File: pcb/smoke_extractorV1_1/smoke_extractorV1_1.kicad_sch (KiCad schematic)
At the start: 25 parts

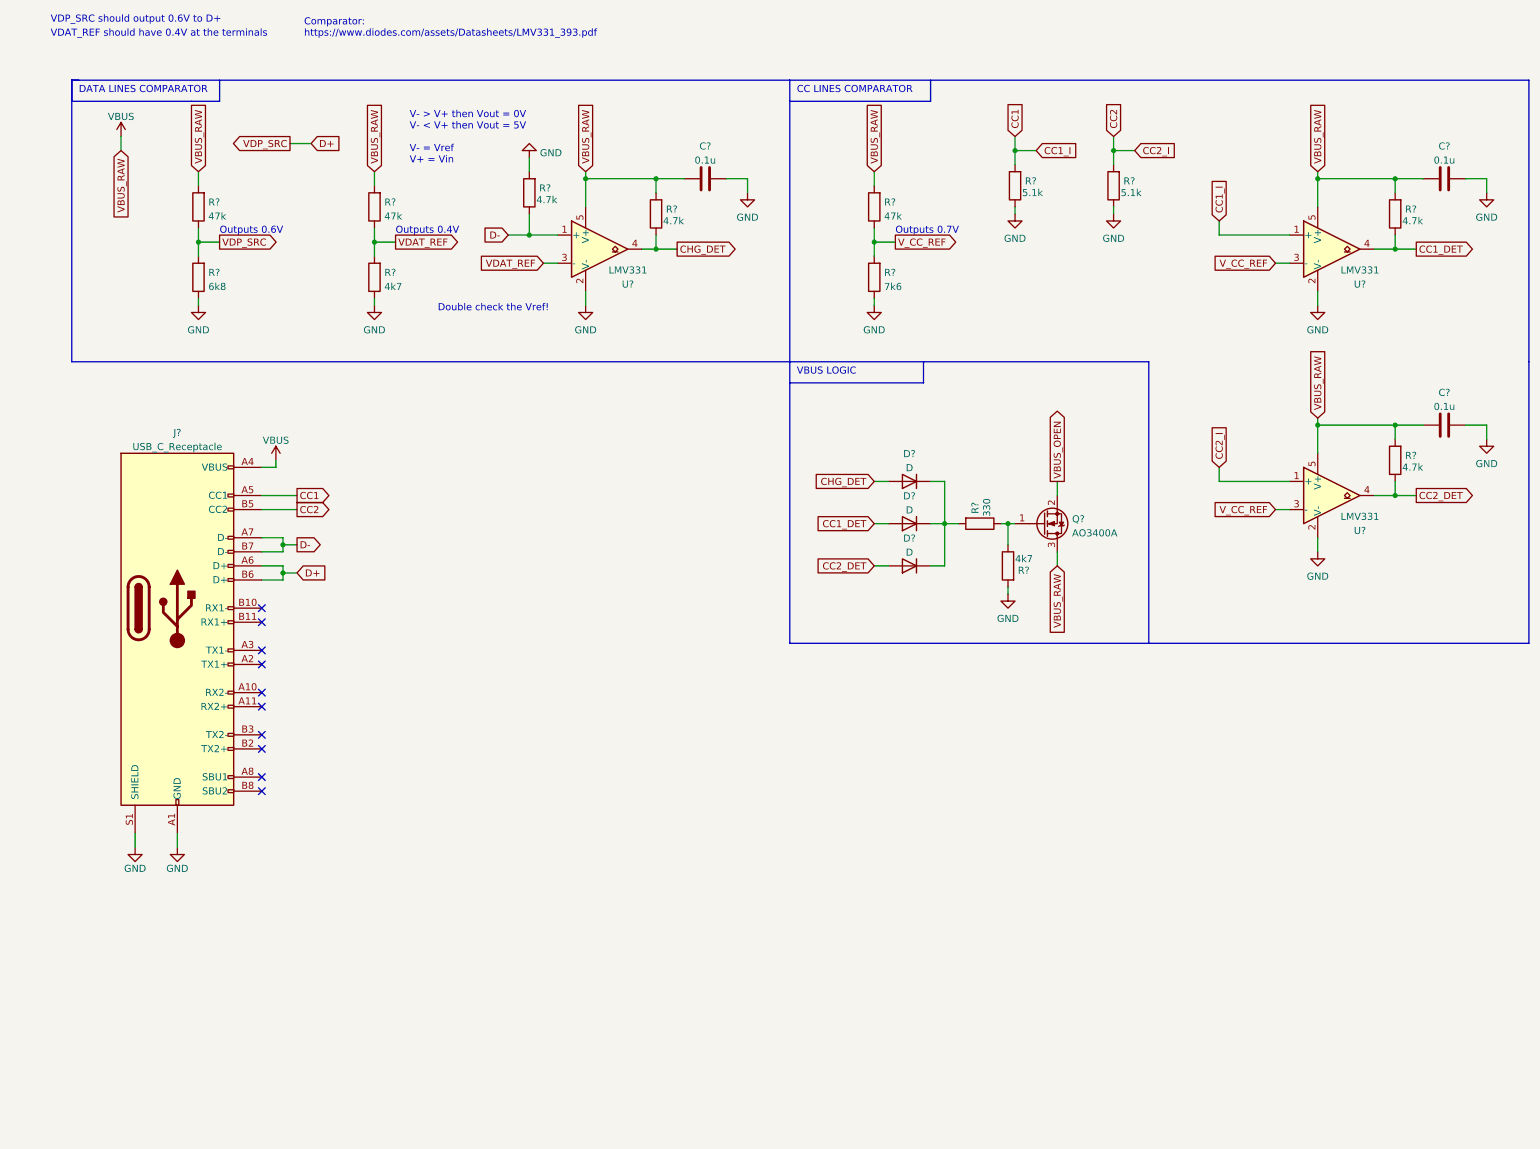
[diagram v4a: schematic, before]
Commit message: Added boost symbol + circuit
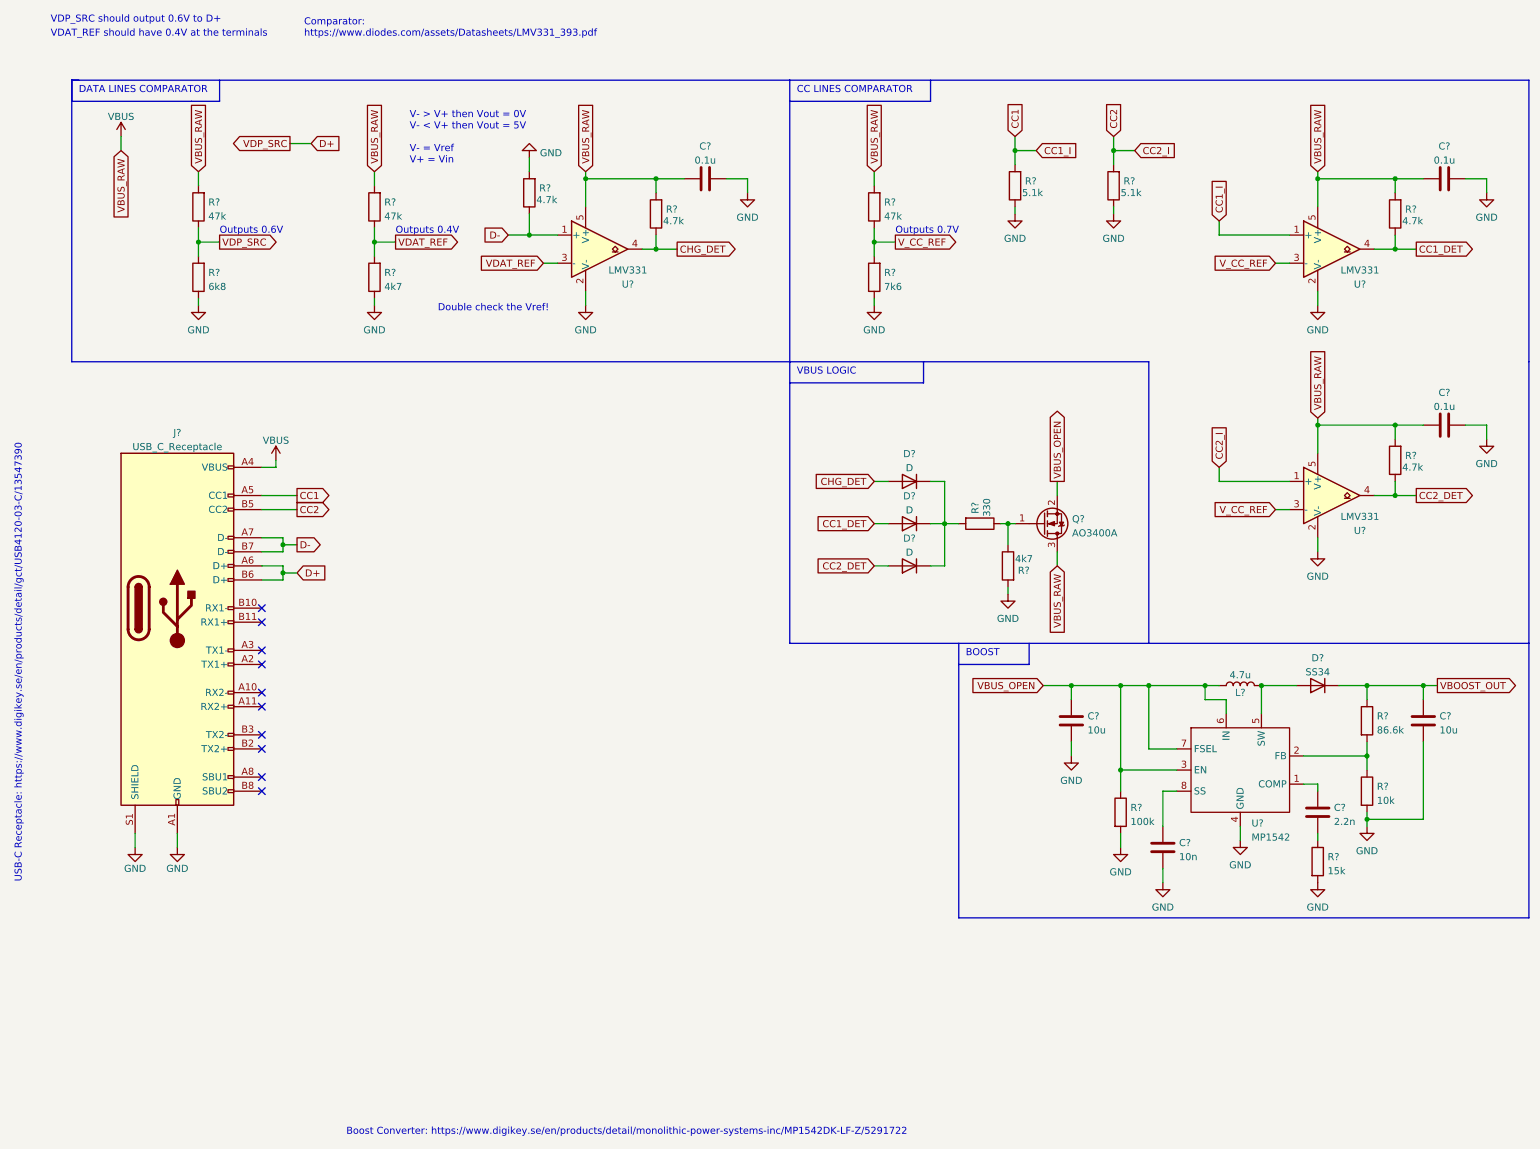
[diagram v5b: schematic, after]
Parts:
- added C?: 2.2n, symbol Device:C
- added C? (x2): 10u, symbol Device:C
- added C?: 10n, symbol Device:C
- added D?: SS34, symbol Device:D
- added L?: 4.7u, symbol Device:L
- added R?: 86.6k, symbol Device:R
- added R?: 15k, symbol Device:R
- added R?: 100k, symbol Device:R
- added R?: 10k, symbol Device:R
- added U?: MP1542, symbol CustomSymbols:MP1542
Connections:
- net GND: now also C?.2, C?.2, C?.2, R?.2, R?.2, R?.2, U?.4 (GND)
- net VBUS_OPEN: now also C?.1, L?.1, R?.1, U?.3 (EN), U?.6 (IN), U?.7 (FSEL)
- new net: C?.1, U?.1 (COMP)
- new net: R?.1, R?.2, U?.2 (FB)
- new net: D?.2 (A), L?.2, U?.5 (SW)
- new net: C?.1, U?.8 (SS)
- new net: C?.2, R?.1
- new net VBOOST_OUT: C?.1, D?.1 (K), R?.1
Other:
- note added: "BOOST"
- note added: "Boost Converter: https://www.digikey.se/en/products/detail/monolithic-power-systems-inc/MP1542DK-LF-Z/5291722"
- note added: "USB-C Receptacle: https://www.digikey.se/en/products/detail/gct/USB4120-03-C/13547390"

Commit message: Final schematics tweaks and BOM
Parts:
- added D?: LED, symbol Device:LED
- added H? (x4): MountingHole_Pad, symbol Mechanical:MountingHole_Pad
- added J?: Screw_Terminal_01x02, symbol Connector:Screw_Terminal_01x02
- added R?: 86.6k, symbol Device:R
- added U?: RA11131100, symbol CustomSymbols:RA11131100
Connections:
- net GND: now also D?.1 (K), H?.1, H?.1, H?.1, H?.1, J?.2 (Pin_2)
- net VBOOST_OUT: now also J?.1 (Pin_1)
- net VBUS_OPEN: now also U?.1 (IN); no longer C?.1, L?.1, R?.1, U?.3 (EN), U?.6 (IN), U?.7 (FSEL)
- new net: D?.2 (A), R?.2
- new net VBUS_SWITCH: C?.1, L?.1, R?.1, R?.1, U?.2 (OUT), U?.3 (EN), U?.6 (IN), U?.7 (FSEL)
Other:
- note added: "MOUNTING HOLES"
- note added: "OUTPUT"
- note added: "SWITCH"
- moved on the sheet: C?

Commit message: Ready to start designing!
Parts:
- C1, C3, C4, C6, C7: renamed from C?; footprint (none) -> Capacitor_SMD:C_0603_1608Metric_Pad1.08x0.95mm_HandSolder
- C2, C5: renamed from C?; footprint (none) -> Capacitor_SMD:C_0805_2012Metric_Pad1.18x1.45mm_HandSolder
- D1, D2, D3: renamed from D?; footprint (none) -> Diode_SMD:D_SOD-523
- D4: renamed from D?; footprint (none) -> LED_SMD:LED_0201_0603Metric_Pad0.64x0.40mm_HandSolder
- D5: renamed from D?; footprint (none) -> Diode_SMD:Nexperia_CFP3_SOD-123W
- H1, H2, H3, H4: renamed from H?; footprint (none) -> MountingHole:MountingHole_3.2mm_M3_ISO7380_Pad
- J1: renamed from J?; footprint (none) -> CustomFootprints:USB4120-03-C
- J2: renamed from J?; footprint (none) -> TerminalBlock:TerminalBlock_bornier-2_P5.08mm
- L1: renamed from L?; footprint (none) -> Inductor_SMD:L_1008_2520Metric_Pad1.43x2.20mm_HandSolder
- R1, R10, R11, R12, R13, R14, R15, R16, R17, R18, R19, R2, R3, R4, R5, R6, R7, R8, R9: renamed from R?; footprint (none) -> Resistor_SMD:R_0603_1608Metric_Pad0.98x0.95mm_HandSolder
- U1, U4, U5: renamed from U?; footprint (none) -> Package_TO_SOT_SMD:SOT-353_SC-70-5_Handsoldering
- U2: renamed from U?; footprint (none) -> CustomFootprints:RA11131100
- U3: renamed from U?; footprint (none) -> Package_SO:MSOP-8_3x3mm_P0.65mm
- gave numbers to parts that had none: 1

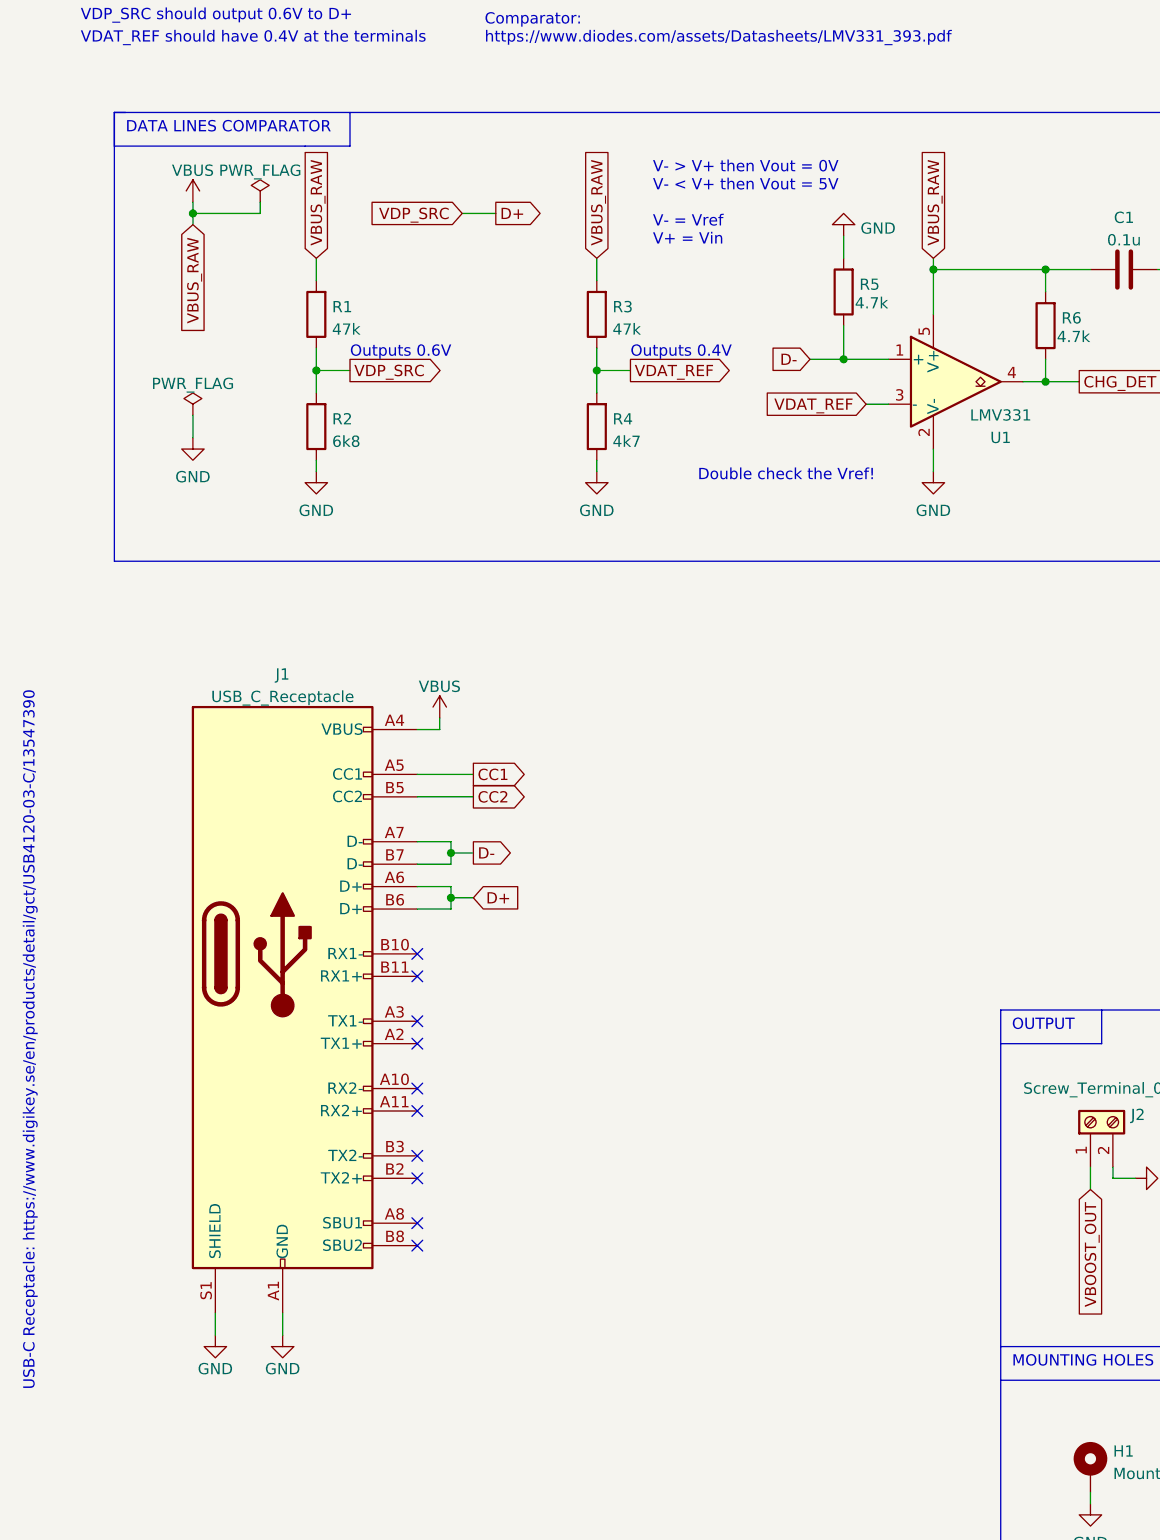
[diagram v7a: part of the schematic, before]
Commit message: Added overvoltage IC
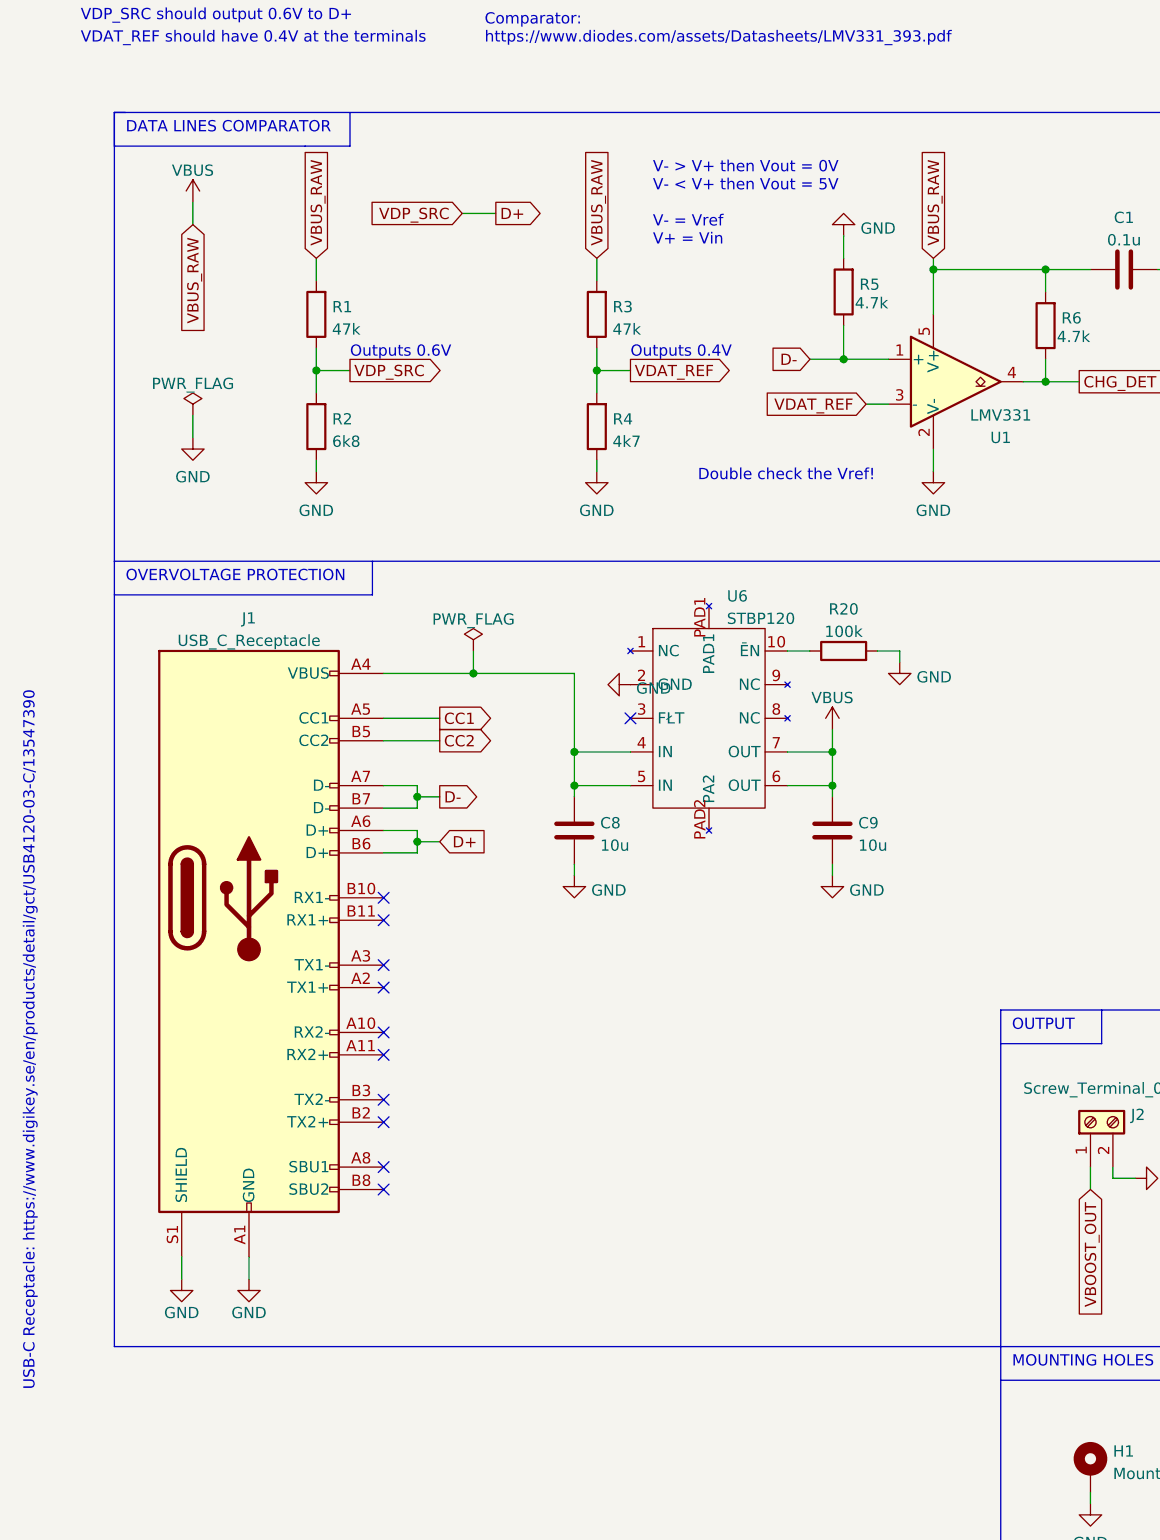
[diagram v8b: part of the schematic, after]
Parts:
- added C8, C9: 10u, Capacitor_SMD:C_0805_2012Metric_Pad1.18x1.45mm_HandSolder, symbol Device:C
- added R20: 100k, Resistor_SMD:R_0603_1608Metric_Pad0.98x0.95mm_HandSolder, symbol Device:R
- added U6: STBP120, Package_DFN_QFN:TDFN-10-1EP_2x3mm_P0.5mm_EP0.9x2mm_ThermalVias, symbol CustomSymbols:STBP120
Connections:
- net GND: now also C8.2, C9.2, R20.2, U6.2 (GND)
- net VBUS: now also C9.1, U6.6 (OUT), U6.7 (OUT); no longer J1.A4 (VBUS), J1.A9 (VBUS), J1.B4 (VBUS), J1.B9 (VBUS)
- new net: C8.1, J1.A4 (VBUS), J1.A9 (VBUS), J1.B4 (VBUS), J1.B9 (VBUS), U6.4 (IN), U6.5 (IN)
- new net: R20.1, U6.10 (ĒN)
- no-connect marks 10 -> 11
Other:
- note added: "OVERVOLTAGE PROTECTION"
- moved on the sheet: J1
